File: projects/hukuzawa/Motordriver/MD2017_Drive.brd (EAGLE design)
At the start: 70 x 70 mm, 20 parts

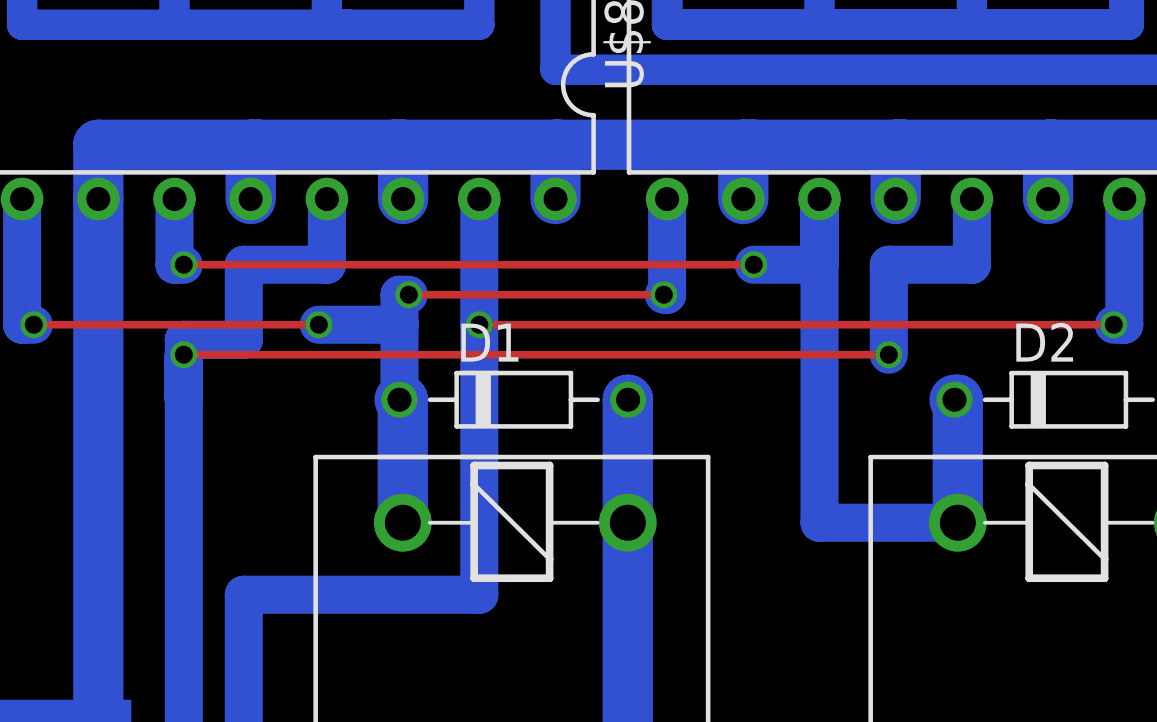
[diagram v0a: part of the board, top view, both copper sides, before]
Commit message: モータードライバ駆動部修正
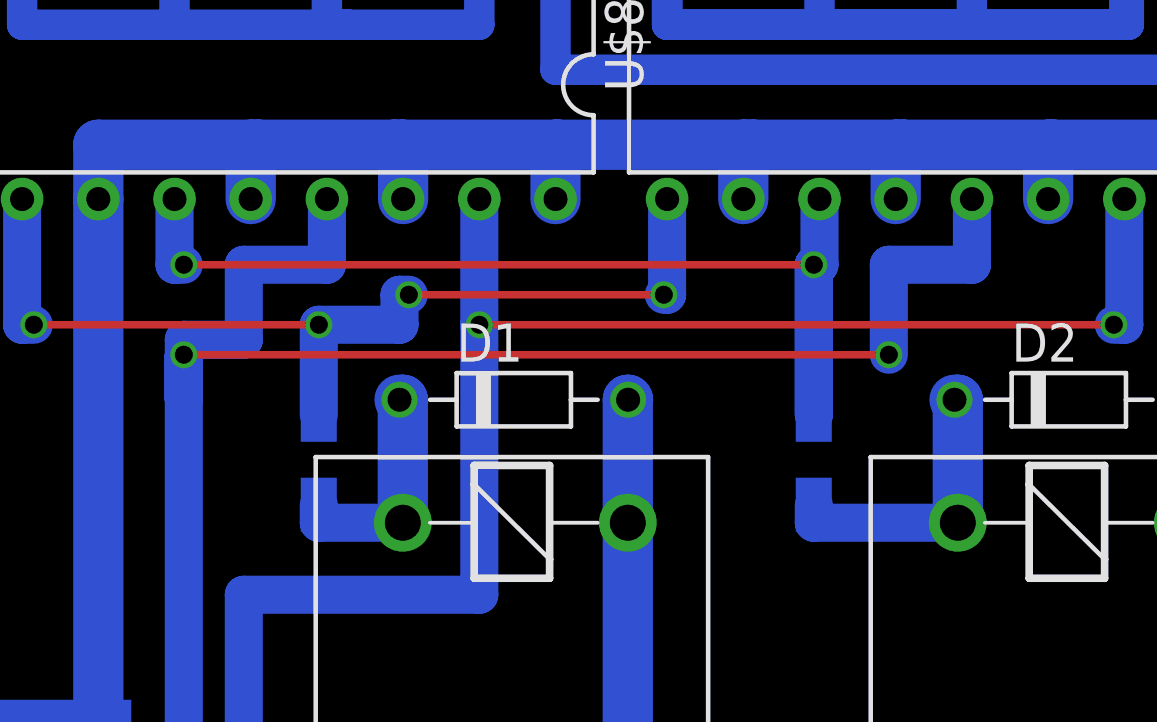
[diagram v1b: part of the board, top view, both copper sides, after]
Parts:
- added R10, R9: (no value), rcl:R3216W
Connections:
- new net 11: D2.PK, R10.1, U$6.1
- new net N$9: D1.PK, R9.1, U$5.1
- net D/B: now also R10.2; no longer D2.PK, U$6.1
- net DIR: now also R9.2; no longer D1.PK, U$5.1
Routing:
- net 11: track 0.00 -> 9.61 mm
- net D/B: track 45.5 -> 35.9 mm
- net N$9: track 0.00 -> 7.61 mm
- net DIR: track 36.6 -> 32.9 mm
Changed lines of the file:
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@@
 <element name="R8" library="rcl" package="R3216W" value="" x="26" y="60.5" rot="MR90"/>
 <element name="U$9" library="Powerio" package="2P" value="2P" x="49.5" y="3" rot="R180"/>
+<element name="R9" library="rcl" package="R3216W" value="" x="25" y="36" rot="MR90"/>
+<element name="R10" library="rcl" package="R3216W" value="" x="41.5" y="36" rot="MR90"/>
 </elements>
 <signals>
@@
 <wire x1="20.5" y1="39.5" x2="44" y2="39.5" width="0.254" layer="1"/>
 </signal>
-<signal name="D/B">
-<contactref element="U$7" pad="11"/>
-<contactref element="U$8" pad="11"/>
-<contactref element="U$6" pad="1"/>
-<contactref element="D2" pad="PK"/>
-<wire x1="46.3" y1="33.9" x2="46.3" y2="38" width="1.6764" layer="16"/>
-<wire x1="46.3" y1="38" x2="46.19" y2="38" width="1.6764" layer="16"/>
-<wire x1="20.19" y1="44.69" x2="20.19" y2="42.5" width="1.27" layer="16"/>
-<wire x1="20.19" y1="42.5" x2="20.5" y2="42.5" width="1.27" layer="16"/>
-<via x="20.5" y="42.5" extent="1-16" drill="0.6" shape="square"/>
-<wire x1="20.5" y1="42.5" x2="39.5" y2="42.5" width="0.254" layer="1"/>
-<via x="39.5" y="42.5" extent="1-16" drill="0.6" shape="square"/>
-<wire x1="39.5" y1="42.5" x2="41.69" y2="42.5" width="1.27" layer="16"/>
-<wire x1="41.69" y1="42.5" x2="41.69" y2="44.69" width="1.27" layer="16"/>
-<wire x1="41.69" y1="44.69" x2="41.69" y2="33.9" width="1.27" layer="16"/>
-<wire x1="41.69" y1="33.9" x2="46.3" y2="33.9" width="1.27" layer="16"/>
-</signal>
 <signal name="DIR">
 <contactref element="U$7" pad="9"/>
 <contactref element="U$8" pad="9"/>
-<contactref element="U$5" pad="1"/>
-<contactref element="D1" pad="PK"/>
-<wire x1="27.8" y1="33.9" x2="27.8" y2="38" width="1.6764" layer="16"/>
-<wire x1="27.8" y1="38" x2="27.69" y2="38" width="1.6764" layer="16"/>
 <via x="25" y="40.5" extent="1-16" drill="0.6" shape="square"/>
 <wire x1="25" y1="40.5" x2="15.5" y2="40.5" width="0.254" layer="1"/>
@@
 <wire x1="15.5" y1="40.5" x2="15.11" y2="40.5" width="1.27" layer="16"/>
 <wire x1="15.11" y1="40.5" x2="15.11" y2="44.69" width="1.27" layer="16"/>
-<wire x1="27.69" y1="38" x2="27.69" y2="40.5" width="1.27" layer="16"/>
 <wire x1="27.69" y1="40.5" x2="27.69" y2="41.5" width="1.27" layer="16"/>
 <wire x1="27.69" y1="41.5" x2="28" y2="41.5" width="1.27" layer="16"/>
@@
 <wire x1="36.61" y1="41.5" x2="36.61" y2="44.69" width="1.27" layer="16"/>
 <wire x1="25" y1="40.5" x2="27.69" y2="40.5" width="1.27" layer="16"/>
+<contactref element="R9" pad="2"/>
+<wire x1="25" y1="37.499" x2="25" y2="40.5" width="1.27" layer="16"/>
 </signal>
 <signal name="GND-D">
@@
 <wire x1="32.89" y1="46.5" x2="33" y2="46.5" width="1.6764" layer="16"/>
 </signal>
+<signal name="N$9">
+<contactref element="U$5" pad="1"/>
+<contactref element="D1" pad="PK"/>
+<contactref element="R9" pad="1"/>
+<wire x1="27.8" y1="33.9" x2="27.8" y2="38" width="1.6764" layer="16"/>
+<wire x1="27.8" y1="38" x2="27.69" y2="38" width="1.6764" layer="16"/>
+<wire x1="25" y1="34.501" x2="25" y2="33.9" width="1.27" layer="16"/>
+<wire x1="25" y1="33.9" x2="27.8" y2="33.9" width="1.27" layer="16"/>
+</signal>
+<signal name="11">
+<contactref element="U$6" pad="1"/>
+<contactref element="D2" pad="PK"/>
+<wire x1="46.3" y1="33.9" x2="46.3" y2="38" width="1.6764" layer="16"/>
+<wire x1="46.3" y1="38" x2="46.19" y2="38" width="1.6764" layer="16"/>
+<contactref element="R10" pad="1"/>
+<wire x1="46.3" y1="33.9" x2="41.5" y2="33.9" width="1.27" layer="16"/>
+<wire x1="41.5" y1="33.9" x2="41.5" y2="34.501" width="1.27" layer="16"/>
+</signal>
+<signal name="D/B">
+<contactref element="R10" pad="2"/>
+<contactref element="U$7" pad="11"/>
+<contactref element="U$8" pad="11"/>
+<wire x1="41.69" y1="44.69" x2="41.69" y2="42.5" width="1.27" layer="16"/>
+<wire x1="41.69" y1="42.5" x2="41.5" y2="42.5" width="1.27" layer="16"/>
+<wire x1="41.5" y1="42.5" x2="41.5" y2="37.499" width="1.27" layer="16"/>
+<wire x1="20.19" y1="44.69" x2="20.19" y2="42.5" width="1.27" layer="16"/>
+<wire x1="20.19" y1="42.5" x2="20.5" y2="42.5" width="1.27" layer="16"/>
+<via x="20.5" y="42.5" extent="1-16" drill="0.6" shape="square"/>
+<wire x1="20.5" y1="42.5" x2="41.5" y2="42.5" width="0.254" layer="1"/>
+<via x="41.5" y="42.5" extent="1-16" drill="0.6" shape="square"/>
+<wire x1="41.5" y1="42.5" x2="41.5" y2="37.499" width="1.27" layer="16"/>
+</signal>
 </signals>

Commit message: モータードライバ駆動部リレー修正
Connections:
- net GND-D: now also U$5.4, U$5.7; no longer U$5.2, U$5.5
- net N$1: now also U$6.2, U$6.7; no longer U$6.4, U$6.5
- net N$2: now also U$5.2, U$5.5; no longer U$5.4, U$5.7
- net N$3: now also U$6.4; no longer U$6.2
- net N$4: now also U$6.5; no longer U$6.7
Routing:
- net GND-D: track 228.1 -> 281.6 mm
- net N$2: track 66.9 -> 60.3 mm
- net N$4: track 23.5 -> 28.7 mm
- net N$6: track 14.7 -> 17.1 mm
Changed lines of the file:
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@@
 <contactref element="D1" pad="PA"/>
 <contactref element="U$5" pad="8"/>
-<contactref element="U$5" pad="2"/>
-<contactref element="U$5" pad="5"/>
 <contactref element="LED1" pad="K"/>
 <contactref element="POWERNPORT" pad="1"/>
@@
 <wire x1="35.3" y1="33.9" x2="35.3" y2="38" width="1.6764" layer="16"/>
 <wire x1="35.3" y1="38" x2="35.31" y2="38" width="1.6764" layer="16"/>
-<wire x1="35.3" y1="8.9" x2="35.3" y2="11" width="1.6764" layer="16"/>
-<wire x1="35.3" y1="11" x2="25" y2="11" width="1.6764" layer="16"/>
-<wire x1="25" y1="11" x2="25" y2="18.9" width="1.6764" layer="16"/>
-<wire x1="25" y1="18.9" x2="27.8" y2="18.9" width="1.6764" layer="16"/>
-<wire x1="27.8" y1="18.9" x2="27.8" y2="24.35" width="1.6764" layer="16"/>
-<wire x1="27.8" y1="24.35" x2="35.5" y2="24.35" width="1.6764" layer="16"/>
-<wire x1="35.5" y1="24.35" x2="54" y2="24.35" width="1.6764" layer="16"/>
-<wire x1="54" y1="24.35" x2="67" y2="24.35" width="1.6764" layer="16"/>
-<wire x1="53.8" y1="33.9" x2="53.8" y2="24.35" width="1.6764" layer="16"/>
-<wire x1="53.8" y1="24.35" x2="54" y2="24.35" width="1.6764" layer="16"/>
-<wire x1="35.3" y1="33.9" x2="35.3" y2="24.35" width="1.6764" layer="16"/>
-<wire x1="35.3" y1="24.35" x2="35.5" y2="24.35" width="1.6764" layer="16"/>
 <wire x1="4" y1="57.27" x2="4" y2="68" width="1.6764" layer="16"/>
 <wire x1="4" y1="68" x2="67" y2="68" width="1.6764" layer="16"/>
 <wire x1="67" y1="68" x2="67" y2="26.89" width="1.6764" layer="16"/>
+<contactref element="U$5" pad="4"/>
+<contactref element="U$5" pad="7"/>
+<wire x1="35.3" y1="33.9" x2="35.3" y2="18.9" width="1.6764" layer="16"/>
+<wire x1="53.8" y1="33.9" x2="53.8" y2="26.89" width="1.6764" layer="16"/>
+<wire x1="53.8" y1="26.89" x2="67" y2="26.89" width="1.6764" layer="16"/>
+<wire x1="35.31" y1="38" x2="35.31" y2="26.89" width="1.6764" layer="16"/>
+<wire x1="35.31" y1="26.89" x2="67" y2="26.89" width="1.6764" layer="16"/>
+<wire x1="27.8" y1="8.9" x2="25" y2="8.9" width="1.6764" layer="16"/>
+<wire x1="25" y1="8.9" x2="25" y2="26.5" width="1.6764" layer="16"/>
+<wire x1="25" y1="26.5" x2="25" y2="26.89" width="1.6764" layer="16"/>
+<wire x1="25" y1="26.89" x2="67" y2="26.89" width="1.6764" layer="16"/>
 </signal>
 <signal name="BDIR">
@@
 <signal name="N$2">
 <contactref element="U$4" pad="5"/>
-<contactref element="U$5" pad="4"/>
-<contactref element="U$5" pad="7"/>
-<wire x1="35.3" y1="18.9" x2="35.3" y2="21.5" width="1.6764" layer="16"/>
-<wire x1="35.3" y1="21.5" x2="40" y2="21.5" width="1.6764" layer="16"/>
-<via x="40" y="21.5" extent="1-16" drill="0.6" shape="square"/>
-<wire x1="40" y1="21.5" x2="40" y2="5" width="0.254" layer="1"/>
-<via x="40" y="5" extent="1-16" drill="0.6" shape="square"/>
-<wire x1="40" y1="5" x2="28" y2="5" width="1.6764" layer="16"/>
-<wire x1="28" y1="5" x2="27.8" y2="5" width="1.6764" layer="16"/>
-<wire x1="27.8" y1="5" x2="27.8" y2="8.9" width="1.6764" layer="16"/>
-<wire x1="9.6" y1="5" x2="28" y2="5" width="1.6764" layer="16"/>
-<wire x1="9.6" y1="5" x2="9" y2="5" width="1.6764" layer="16"/>
-<wire x1="9" y1="5" x2="9" y2="12" width="1.6764" layer="16"/>
-<wire x1="9" y1="12" x2="9" y2="12.4" width="0.6096" layer="16"/>
-<wire x1="9" y1="12.4" x2="9.6" y2="12.4" width="0.6096" layer="16"/>
+<contactref element="U$5" pad="5"/>
+<contactref element="U$5" pad="2"/>
+<wire x1="35.3" y1="8.9" x2="35.3" y2="9" width="1.6764" layer="16"/>
+<wire x1="35.3" y1="9" x2="39.5" y2="9" width="1.6764" layer="16"/>
+<via x="39.5" y="9" extent="1-16" drill="0.6" shape="square"/>
+<wire x1="39.5" y1="9" x2="39.5" y2="16.5" width="0.254" layer="1"/>
+<via x="39.5" y="16.5" extent="1-16" drill="0.6" shape="square"/>
+<wire x1="39.5" y1="16.5" x2="27.8" y2="16.5" width="1.6764" layer="16"/>
+<wire x1="27.8" y1="16.5" x2="27.8" y2="18.9" width="1.6764" layer="16"/>
+<wire x1="9.6" y1="12.4" x2="9.5" y2="12.4" width="1.016" layer="16"/>
+<wire x1="9.5" y1="12.4" x2="9.5" y2="12.5" width="1.016" layer="16"/>
+<wire x1="9.5" y1="12.5" x2="9.5" y2="6.5" width="1.6764" layer="16"/>
+<wire x1="9.5" y1="6.5" x2="35" y2="6.5" width="1.6764" layer="16"/>
+<wire x1="35" y1="6.5" x2="35.3" y2="6.5" width="1.6764" layer="16"/>
+<wire x1="35.3" y1="6.5" x2="35.3" y2="8.9" width="1.6764" layer="16"/>
 </signal>
 <signal name="N$3">
 <contactref element="U$5" pad="3"/>
-<contactref element="U$6" pad="2"/>
-<wire x1="46.3" y1="18.9" x2="38.5" y2="18.9" width="1.6764" layer="16"/>
-<wire x1="38.5" y1="18.9" x2="38.5" y2="16" width="1.6764" layer="16"/>
-<wire x1="38.5" y1="16" x2="27.8" y2="16" width="1.6764" layer="16"/>
-<wire x1="27.8" y1="16" x2="27.8" y2="13.9" width="1.6764" layer="16"/>
+<contactref element="U$6" pad="4"/>
+<wire x1="27.8" y1="13.9" x2="27.8" y2="11.5" width="1.6764" layer="16"/>
+<wire x1="27.8" y1="11.5" x2="46" y2="11.5" width="1.6764" layer="16"/>
+<wire x1="46" y1="11.5" x2="46.3" y2="11.5" width="1.6764" layer="16"/>
+<wire x1="46.3" y1="11.5" x2="46.3" y2="8.9" width="1.6764" layer="16"/>
 </signal>
 <signal name="N$4">
 <contactref element="U$5" pad="6"/>
-<contactref element="U$6" pad="7"/>
 <wire x1="35.3" y1="13.9" x2="43" y2="13.9" width="1.6764" layer="16"/>
 <wire x1="43" y1="13.9" x2="43" y2="16.5" width="1.6764" layer="16"/>
-<wire x1="43" y1="16.5" x2="53.8" y2="16.5" width="1.6764" layer="16"/>
-<wire x1="53.8" y1="16.5" x2="53.8" y2="18.9" width="1.6764" layer="16"/>
-</signal>
-<signal name="N$1">
-<contactref element="U$6" pad="4"/>
 <contactref element="U$6" pad="5"/>
-<wire x1="46.3" y1="8.9" x2="53.8" y2="8.9" width="1.6764" layer="16"/>
+<wire x1="43" y1="16.5" x2="51" y2="16.5" width="1.6764" layer="16"/>
+<wire x1="51" y1="16.5" x2="51" y2="9" width="1.6764" layer="16"/>
+<wire x1="51" y1="9" x2="51" y2="8.9" width="1.6764" layer="16"/>
+<wire x1="51" y1="8.9" x2="53.8" y2="8.9" width="1.6764" layer="16"/>
 </signal>
 <signal name="N$5">
@@
 <contactref element="U$9" pad="P2"/>
 <contactref element="U$6" pad="3"/>
-<wire x1="46.3" y1="13.9" x2="46.3" y2="11.5" width="1.6764" layer="16"/>
-<wire x1="46.3" y1="11.5" x2="43.5" y2="11.5" width="1.6764" layer="16"/>
-<wire x1="43.5" y1="11.5" x2="43.5" y2="3" width="1.6764" layer="16"/>
-<wire x1="43.5" y1="3" x2="44.5" y2="3" width="1.6764" layer="16"/>
+<wire x1="46.3" y1="13.9" x2="48.5" y2="13.9" width="1.6764" layer="16"/>
+<wire x1="48.5" y1="13.9" x2="48.5" y2="3" width="1.6764" layer="16"/>
+<wire x1="48.5" y1="3" x2="44.5" y2="3" width="1.6764" layer="16"/>
 </signal>
 <signal name="N$7">
@@
 <wire x1="41.5" y1="42.5" x2="41.5" y2="37.499" width="1.27" layer="16"/>
 </signal>
+<signal name="N$1">
+<contactref element="U$6" pad="2"/>
+<contactref element="U$6" pad="7"/>
+<wire x1="46.3" y1="18.9" x2="53.8" y2="18.9" width="1.6764" layer="16"/>
+</signal>
 </signals>

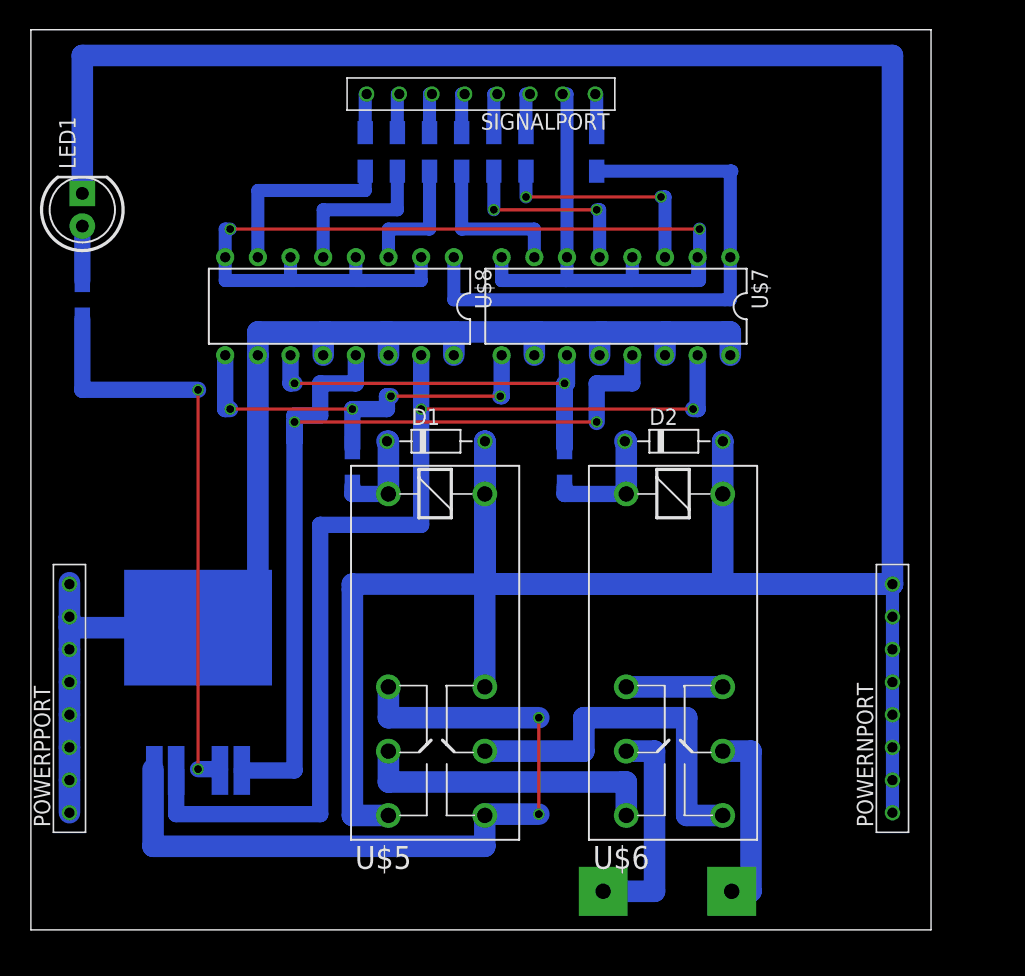
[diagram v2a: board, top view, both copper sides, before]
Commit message: モータードライバ修正
モータードライバのジャンパ線部のドリル径を修正
それに伴って一部の配置の修正
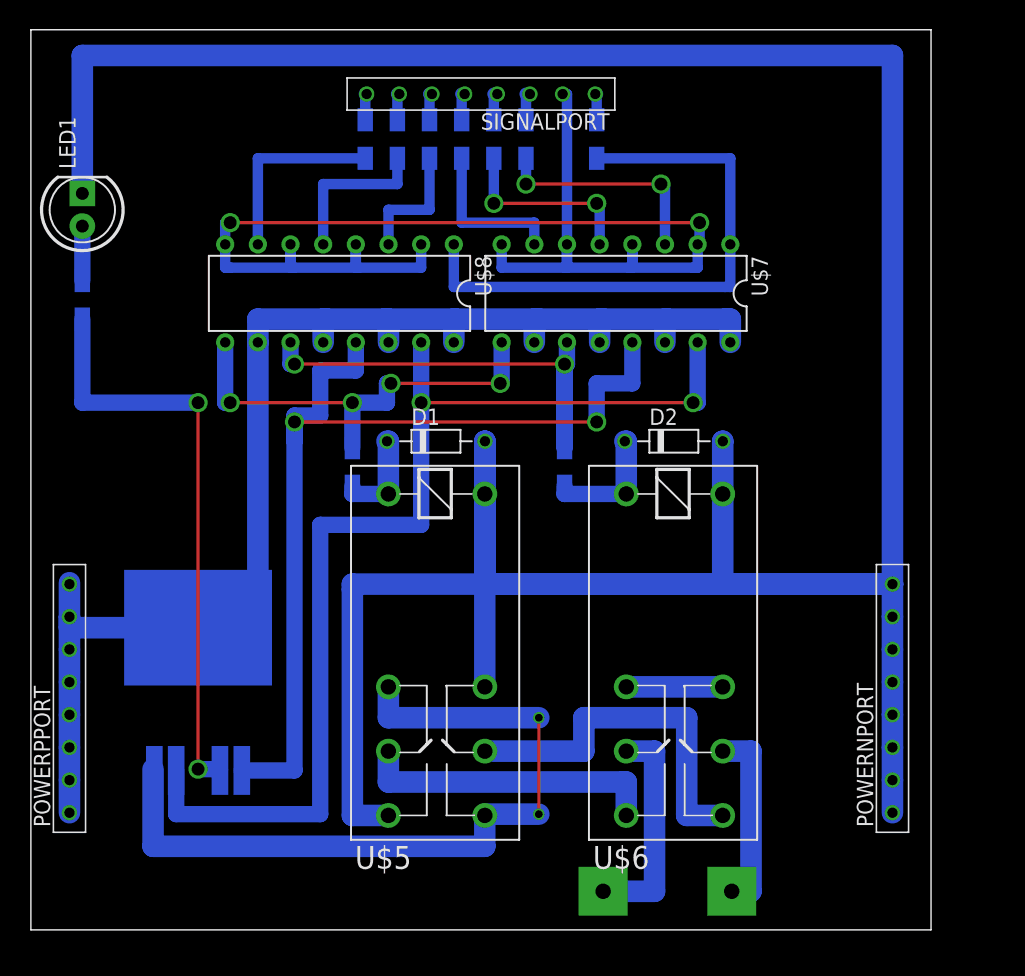
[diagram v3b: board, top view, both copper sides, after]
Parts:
- moved R2 1.00 mm to (44.0, 61.5)
- moved R3 1.00 mm to (38.5, 61.5)
- moved R4 1.00 mm to (36.0, 61.5)
- moved R5 1.00 mm to (33.5, 61.5)
- moved R6 1.00 mm to (31.0, 61.5)
- moved R7 1.00 mm to (28.5, 61.5)
- moved R8 1.00 mm to (26.0, 61.5)
- moved U$7 1.00 mm to (45.5, 49.5)
- moved U$8 1.00 mm to (24.0, 49.5)
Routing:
- net GND-C: track 124.8 -> 104.7 mm
- net N$10: track 84.8 -> 86.8 mm
- net PWM: track 77.1 -> 79.1 mm
- net D/B: track 35.9 -> 37.9 mm
- net DIR: track 32.9 -> 34.4 mm
- net VCC5V: track 3.11 -> 2.11 mm
- net VCC12V: track 107.4 -> 108.4 mm
- net BPWM: track 3.19 -> 2.19 mm
- net BDIR: track 3.11 -> 2.11 mm
- net BD/B: track 3.15 -> 2.15 mm
- net APWM: track 3.31 -> 2.31 mm
- net ADIR: track 3.23 -> 2.23 mm
- net AD/B: track 3.27 -> 2.27 mm
